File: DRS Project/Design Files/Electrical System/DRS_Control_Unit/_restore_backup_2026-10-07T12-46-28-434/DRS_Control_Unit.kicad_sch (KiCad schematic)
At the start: 47 parts, among them IC1 AP63301QWU-7, J1 Screw, J2 Deutsch DT, J3 Servo, J4 DE9_Socket, SW1 DSIC01THGET, U1 AMS1117, U2 Teensy4.0-NU-Teams, U3 TJA1051T-3, U4 LM2596S-ADJ

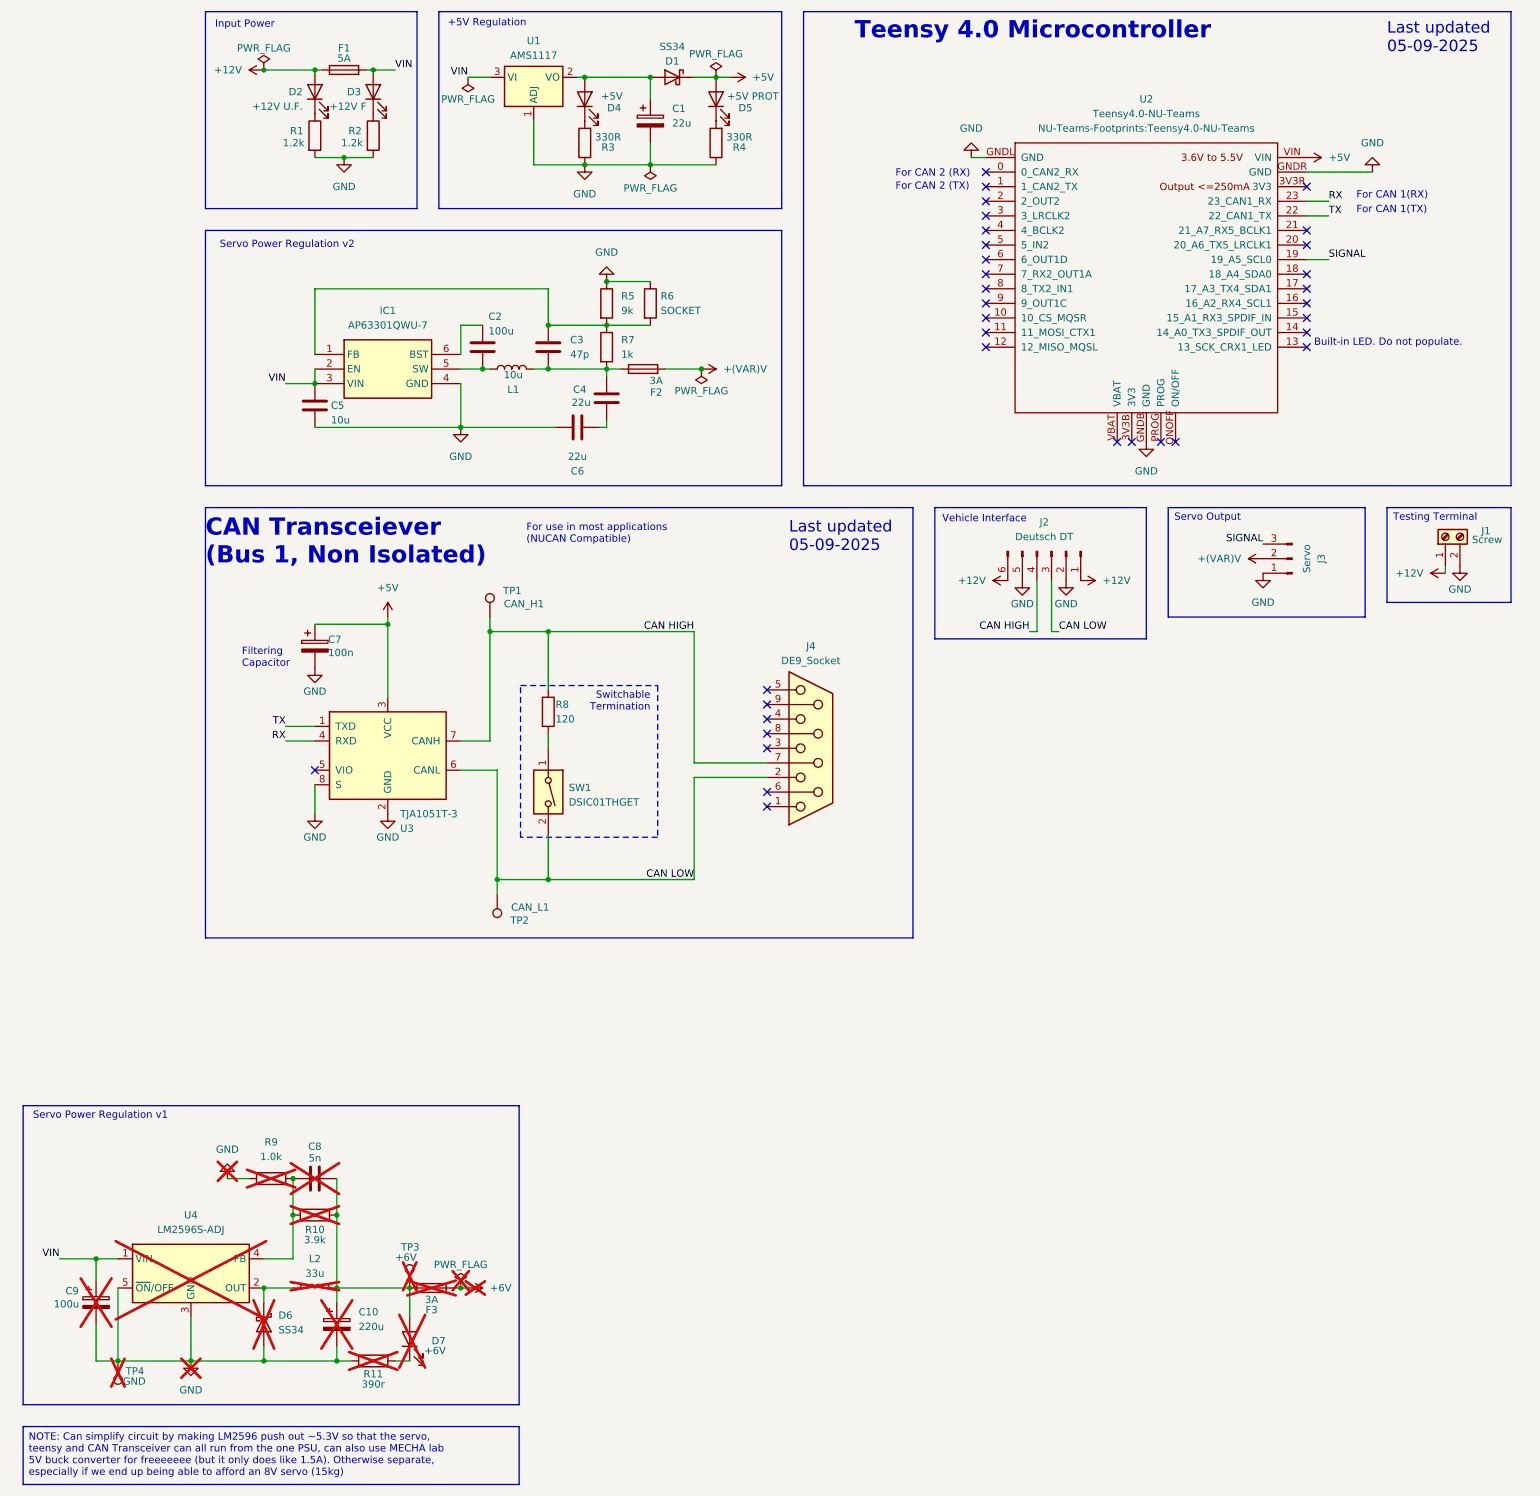
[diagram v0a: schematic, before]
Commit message: DDR started and circuit edited to fit DDR
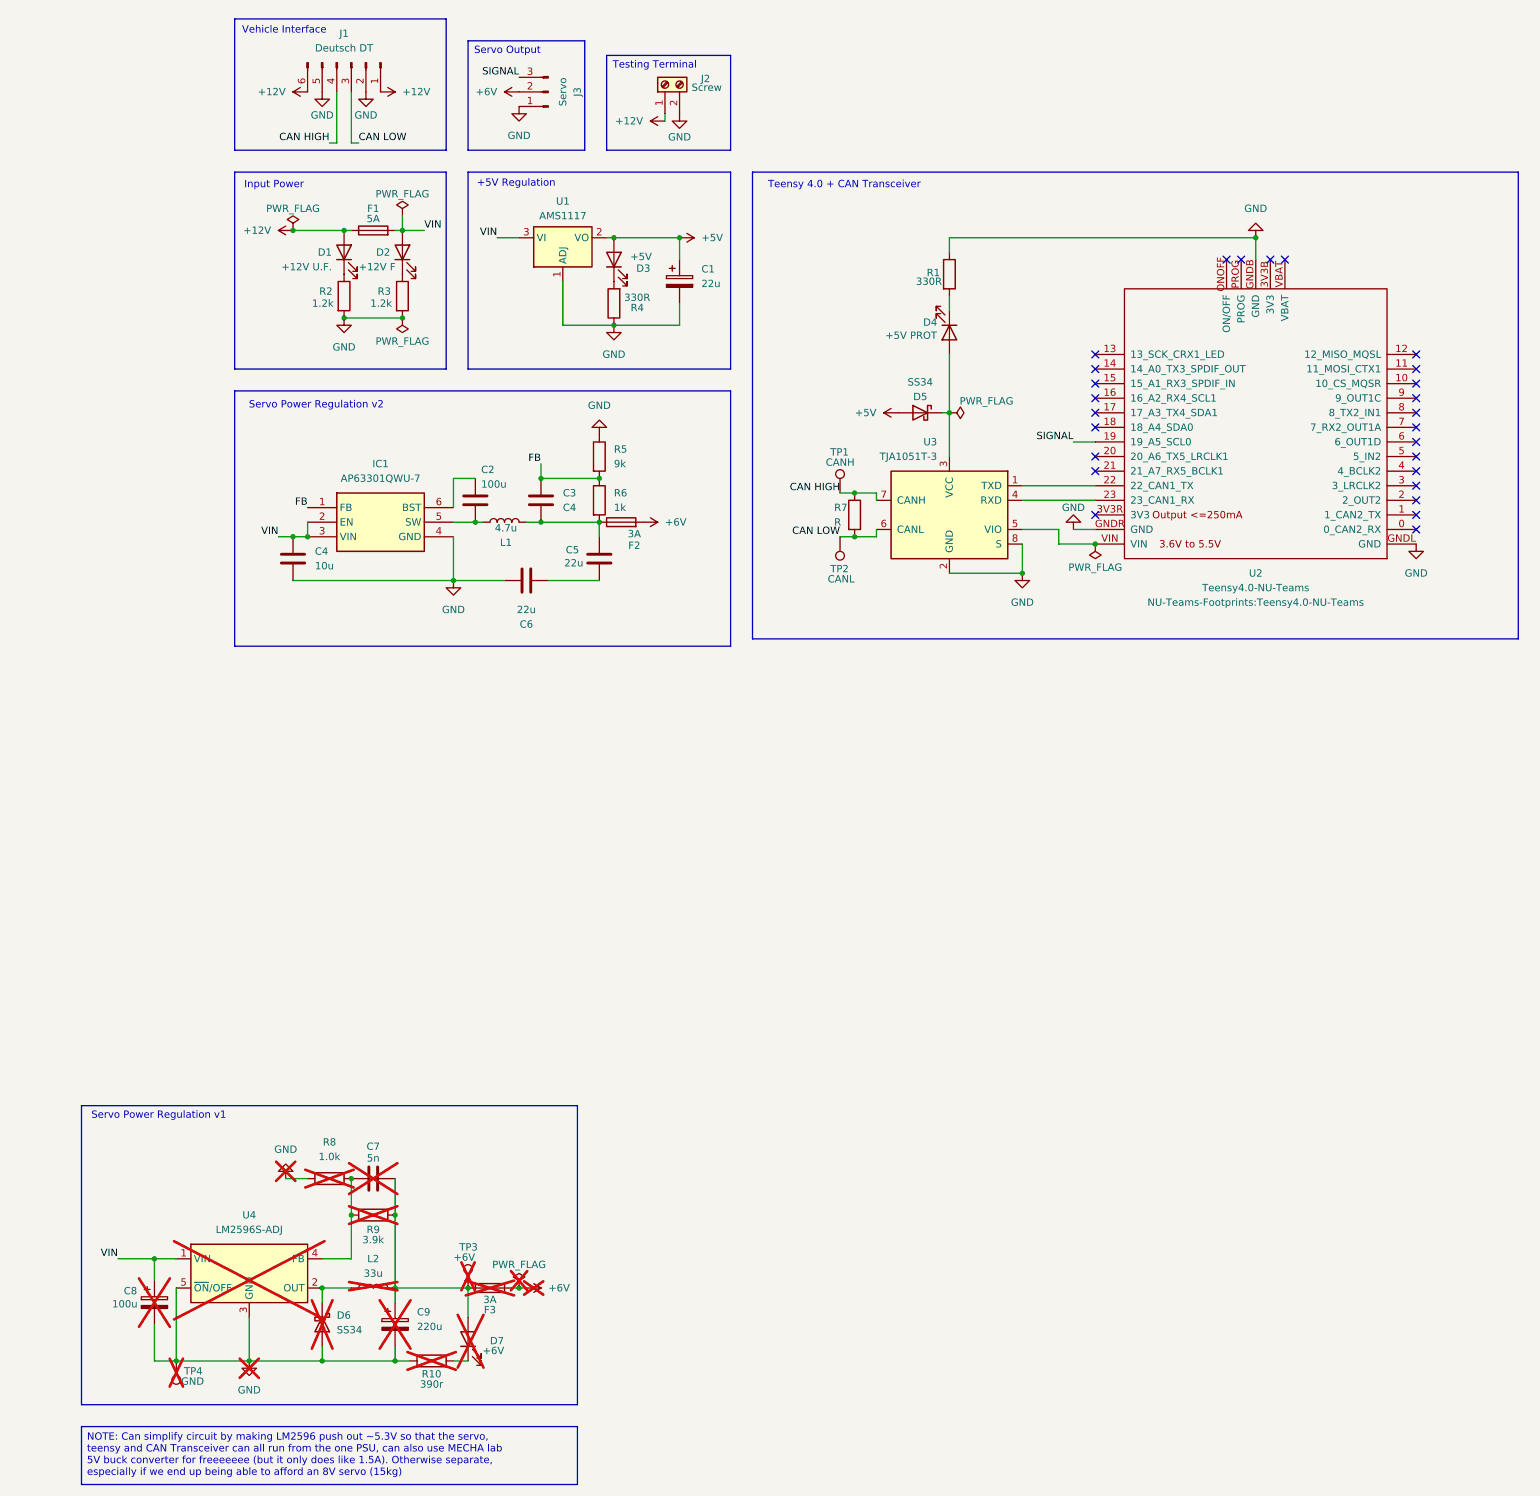
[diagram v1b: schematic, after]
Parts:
- removed C7: 100n, Capacitor_SMD:C_1206_3216Metric, symbol Device:C_Polarized
- removed D1: SS34, Diode_SMD:D_SMA_Handsoldering, symbol Device:D_Schottky
- removed D5: +5V PROT, LED_SMD:LED_1206_3216Metric_Pad1.42x1.75mm_HandSolder, symbol Device:LED
- removed J4: DE9_Socket, Connector_Dsub:DSUB-9_Socket_Vertical_P2.77x2.84mm, symbol Connector:DE9_Socket
- removed R4: 330R, Resistor_SMD:R_1206_3216Metric_Pad1.30x1.75mm_HandSolder, symbol Device:R
- removed R5: 9k, Connector_PinSocket_2.54mm:PinSocket_1x02_P2.54mm_Vertical, symbol Device:R
- removed R8: 120, Resistor_SMD:R_1206_3216Metric_Pad1.30x1.75mm_HandSolder, symbol Device:R
- removed SW1: DSIC01THGET, Button_Switch_THT:SW_DIP_SPSTx01_Slide_6.7x4.1mm_W7.62mm_P2.54mm_LowProfile, symbol Switch:SW_DIP_x01
- added D4: +5V PROT, LED_SMD:LED_1206_3216Metric_Pad1.42x1.75mm_HandSolder, symbol Device:LED
- added D5: SS34, Diode_SMD:D_SMA_Handsoldering, symbol Device:D_Schottky
- added R1: 330R, Resistor_SMD:R_1206_3216Metric_Pad1.30x1.75mm_HandSolder, symbol Device:R
- added R7: R, Connector_PinSocket_2.54mm:PinSocket_1x02_P2.54mm_Vertical, symbol Device:R
- C3: value 47p -> C4
- J1: renamed from J2; footprint TerminalBlock_Phoenix:TerminalBlock_Phoenix_MKDS-1,5-2_1x02_P5.00mm_Horizontal -> NU-Teams-Footprints:DT15-6P
- J2: renamed from J1; footprint NU-Teams-Footprints:DT15-6P -> TerminalBlock_Phoenix:TerminalBlock_Phoenix_MKDS-1,5-2_1x02_P5.00mm_Horizontal
- L1: value 10u -> 4.7u
- R5: renamed from R6; value SOCKET -> 9k; footprint Resistor_SMD:R_1206_3216Metric_Pad1.30x1.75mm_HandSolder -> Connector_PinSocket_2.54mm:PinSocket_1x02_P2.54mm_Vertical
- R6: renamed from R7; footprint Resistor_SMD:R_1206_3216Metric -> Resistor_SMD:R_1206_3216Metric_Pad1.30x1.75mm_HandSolder
- TP1: value CAN_H1 -> CANH; footprint TestPoint:TestPoint_Loop_D1.80mm_Drill1.0mm_Beaded -> TestPoint:TestPoint_THTPad_D2.0mm_Drill1.0mm
- TP2: value CAN_L1 -> CANL; footprint TestPoint:TestPoint_Loop_D1.80mm_Drill1.0mm_Beaded -> TestPoint:TestPoint_THTPad_D2.0mm_Drill1.0mm
- renumbered C5 to C4, C4 to C5, C8 to C7, C9 to C8, C10 to C9, D2 to D1, D3 to D2, D4 to D3, R11 to R10, R1 to R2, R2 to R3, R3 to R4, R9 to R8, R10 to R9
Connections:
- net +(VAR)V is gone; now on net +6V: F2.2, J3.2 (Pin_2)
- net +5V: now also C1.1, D3.2 (A), U1.2 (VO), D5.2 (A); no longer U2.VIN, U3.3 (VCC)
- net CAN HIGH: now also R7.1
- net CAN LOW: now also R7.2
- net GND: now also R1.1
- net FB: now reaches C3.1, IC1.1 (FB), R5.2, R6.1
- net at U3.5 (VIO): now also U2.VIN
- net RX: no longer names the net of U2.23 (23_CAN1_RX), U3.4 (RXD)
- net TX: no longer names the net of U2.22 (22_CAN1_TX), U3.1 (TXD)
- new net: D4.2 (A), D5.1 (K), U3.3 (VCC)
- new net: D4.1 (K), R1.2
- no-connect marks 34 -> 26
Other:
- note added: "Teensy 4.0 + CAN Transceiver"
- note removed: "Built-in LED. Do not populate."
- note removed: "CAN Transceiever (Bus 1, Non Isolated)"
- note removed: "Filtering Capacitor"
- note removed: "For CAN 1(RX)"
- note removed: "For CAN 1(TX)"
- note removed: "For CAN 2 (RX)"
- note removed: "For CAN 2 (TX)"
- note removed: "For use in most applications (NUCAN Compatible)"
- note removed: "Last updated 05-09-2025"
- note removed: "Switchable Termination"
- note removed: "Teensy 4.0 Microcontroller"
- moved on the sheet: C1, C2, C3, C4, C5, C6, C7, C8, C9, D1, D2, D3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
